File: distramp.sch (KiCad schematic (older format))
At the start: 23 parts

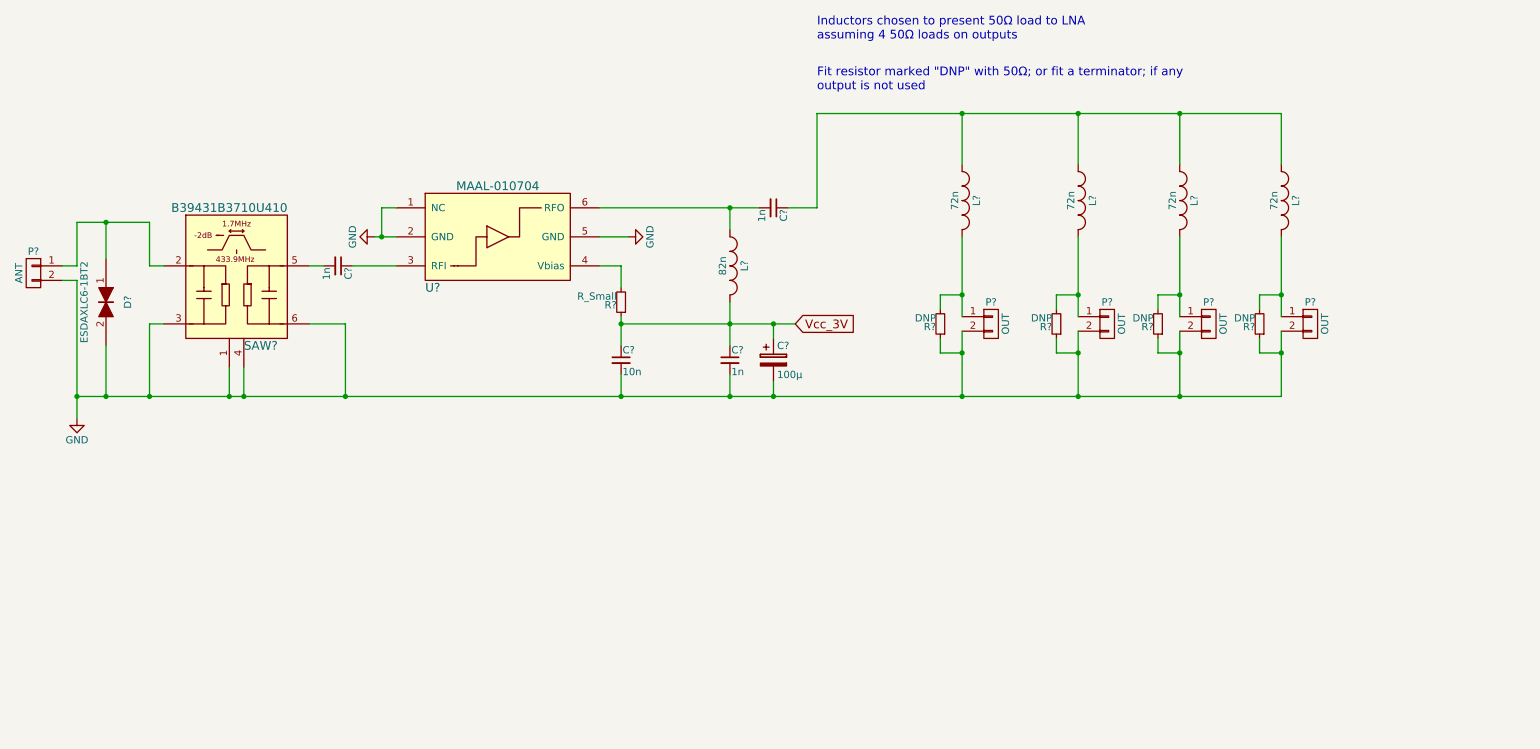
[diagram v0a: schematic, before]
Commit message: Assign footprints, place parts on PCB
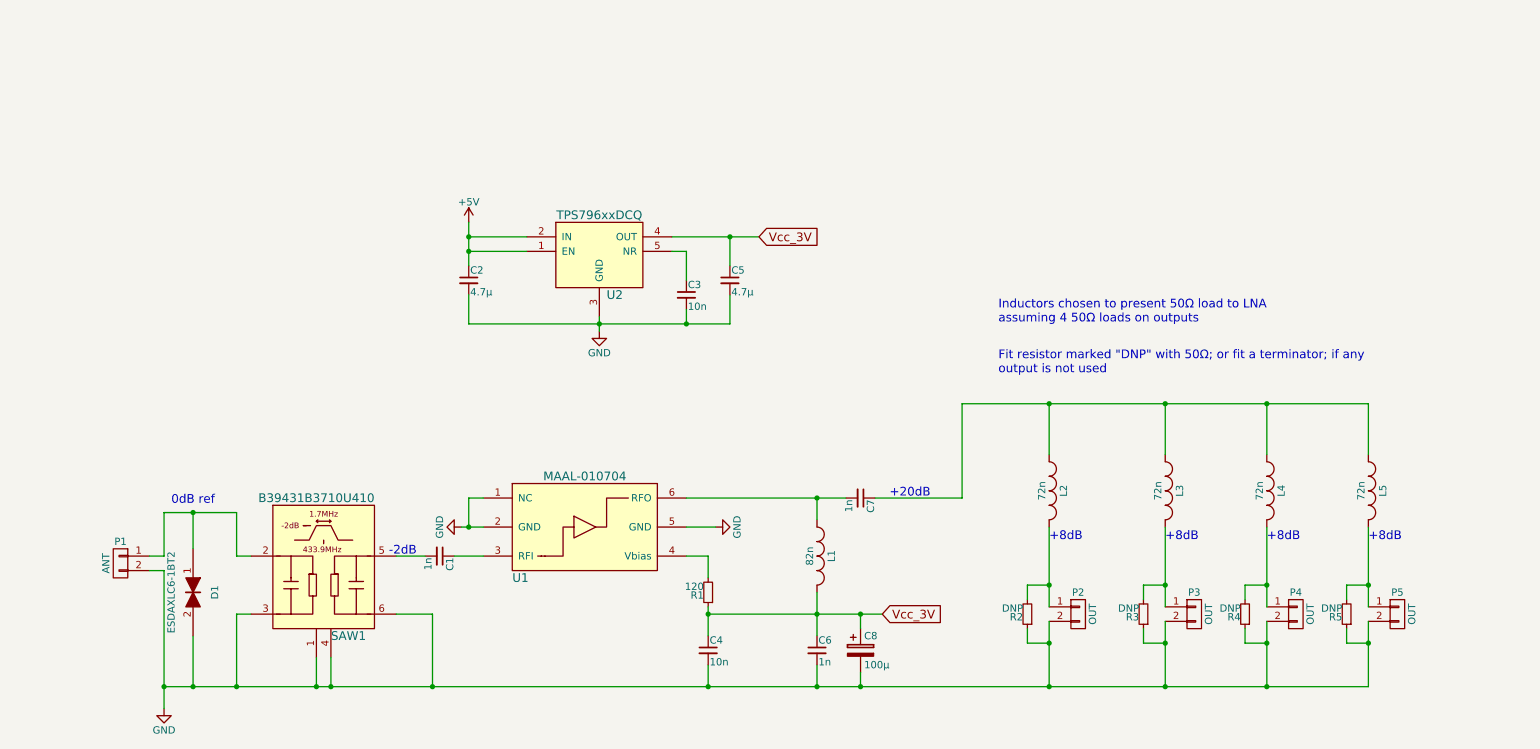
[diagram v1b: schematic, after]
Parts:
- added C2, C5: 4.7µ, Capacitors_SMD:C_0805, symbol C_Small
- added C3: 10n, Capacitors_SMD:C_0402, symbol C_Small
- added U2: TPS796xxDCQ, Custom Parts:SOT-223-6, symbol TPS796xxDCQ
- C1, C4, C6, C7: renamed from C?; footprint (none) -> Capacitors_SMD:C_0402
- C8: renamed from C?; footprint (none) -> Capacitors_Tantalum_SMD:TantalC_SizeD_EIA-7343_Reflow
- D1: renamed from D?; footprint (none) -> Resistors_SMD:R_0402
- L1, L2, L3, L4, L5: renamed from L?; footprint (none) -> Resistors_SMD:R_0402
- P1, P2, P3, P4, P5: renamed from P?; footprint (none) -> Custom Parts:RFcon
- R1: renamed from R?; value R_Small -> 120; footprint (none) -> Resistors_SMD:R_0402
- R2, R3, R4, R5: renamed from R?; footprint (none) -> Resistors_SMD:R_0402
- SAW1: renamed from SAW?; footprint (none) -> Custom Parts:SAW-DCC6C
- U1: renamed from U?; footprint (none) -> TO_SOT_Packages_SMD:SC-70-6_Handsoldering
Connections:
- net GND: now also C2.2, C3.2, C5.2, U2.3 (GND)
- net Vcc_3V: now also C5.1, U2.4 (OUT)
- new net: C3.1, U2.5 (NR)
- new net +5V: C2.1, U2.1 (EN), U2.2 (IN)
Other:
- note added: "+20dB"
- note added: "+8dB"
- note added: "-2dB"
- note added: "0dB ref"
- moved on the sheet: C1, C4, C6, C7, C8, D1, L1, L2, L3, L4, L5, P1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

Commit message: Add Power Connector
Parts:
- added P6: PWR, Pin_Headers:Pin_Header_Straight_1x02, symbol CONN_01X02
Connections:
- net +5V: now also P6.1 (P1)
- net GND: now also P6.2 (P2)
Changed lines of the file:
@@
 	3900 2650 3900 2950
 Wire Wire Line
-	3900 2750 4300 2750
+	3000 2750 4300 2750
 Wire Wire Line
 	3900 2850 4300 2850
@@
 	3900 3150 3900 3350
 Wire Wire Line
-	3900 3350 5700 3350
+	3000 3350 5700 3350
 Wire Wire Line
 	4800 3300 4800 3400
@@
 Vcc_3V
 Connection ~ 5700 2750
+$Comp
+L CONN_01X02 P6
+U 1 1 578673A9
+P 2700 2900
+F 0 "P6" H 2700 3050 50  0000 C CNN
+F 1 "PWR" V 2800 2900 50  0000 C CNN
+F 2 "Pin_Headers:Pin_Header_Straight_1x02" H 2700 2900 50  0001 C CNN
+F 3 "" H 2700 2900 50  0000 C CNN
+	1    2700 2900
+	-1   0    0    -1
+$EndComp
+Wire Wire Line
+	2900 2850 3000 2850
+Wire Wire Line
+	3000 2850 3000 2750
+Wire Wire Line
+	3000 3350 3000 2950
+Wire Wire Line
+	3000 2950 2900 2950
+Connection ~ 3900 3350
 $EndSCHEMATC

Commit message: Specify 869MHz component values
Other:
- note added: "36n"
- note added: "B39871B3725U410"
- note added: "Component values in dashed boxes\nare for 869MHz version."
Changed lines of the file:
@@
 encoding utf-8
 Sheet 1 1
-Title "434MHz LNA/Distribution Amp"
+Title "434MHz/869MHz LNA/Distribution Amp"
 Date "2016-07-12"
 Rev "1"
@@
 	3000 2950 2900 2950
 Connection ~ 3900 3350
+Text Notes 2425 4450 0    60   ~ 0
+B39871B3725U410
+Wire Notes Line
+	2400 4475 3300 4475
+Wire Notes Line
+	3300 4475 3300 4350
+Wire Notes Line
+	3300 4350 2400 4350
+Wire Notes Line
+	2400 4350 2400 4475
+Text Notes 7775 4575 1    50   ~ 0
+36n
+Wire Notes Line
+	7675 4600 7800 4600
+Wire Notes Line
+	7800 4600 7800 4425
+Wire Notes Line
+	7800 4425 7675 4425
+Wire Notes Line
+	7675 4425 7675 4600
+Text Notes 8575 4575 1    50   ~ 0
+36n
+Wire Notes Line
+	8475 4600 8600 4600
+Wire Notes Line
+	8600 4600 8600 4425
+Wire Notes Line
+	8600 4425 8475 4425
+Wire Notes Line
+	8475 4425 8475 4600
+Text Notes 9275 4575 1    50   ~ 0
+36n
+Wire Notes Line
+	9175 4600 9300 4600
+Wire Notes Line
+	9300 4600 9300 4425
+Wire Notes Line
+	9300 4425 9175 4425
+Wire Notes Line
+	9175 4425 9175 4600
+Text Notes 9975 4575 1    50   ~ 0
+36n
+Wire Notes Line
+	9875 4600 10000 4600
+Wire Notes Line
+	10000 4600 10000 4425
+Wire Notes Line
+	10000 4425 9875 4425
+Wire Notes Line
+	9875 4425 9875 4600
+Text Notes 7550 3025 0    60   ~ 0
+Component values in dashed boxes\nare for 869MHz version.
 $EndSCHEMATC
